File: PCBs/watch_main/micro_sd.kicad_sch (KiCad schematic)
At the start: 2 parts, among them IC1002 NVT4858HKZ, J1101 105162-0001

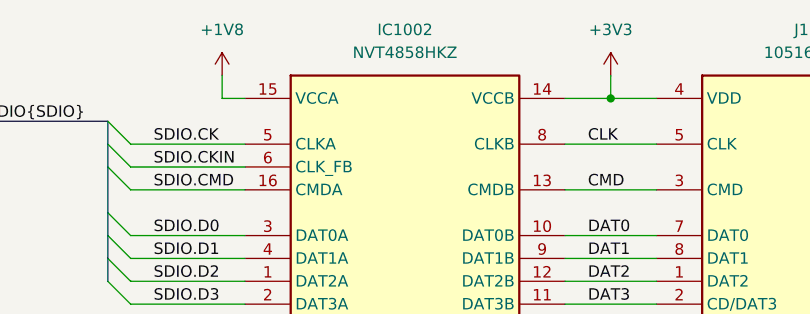
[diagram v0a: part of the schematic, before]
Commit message: Created firmware project
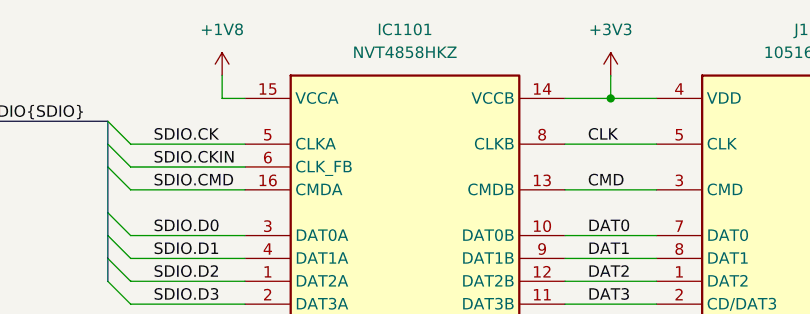
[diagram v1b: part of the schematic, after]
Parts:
- renumbered IC1002 to IC1101
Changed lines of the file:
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@@
   (symbol (lib_id "NVT4858HKZ:NVT4858HKZ") (at 142.24 71.12 0) (unit 1)
     (in_bom yes) (on_board yes) (dnp no)
-    (property "Reference" "IC1002" (at 142.24 50.8 0)
+    (property "Reference" "IC1101" (at 142.24 50.8 0)
       (effects (font (size 1.27 1.27)))
     )
@@
       (project "watch_main"
         (path "/b008648a-c7cf-4e14-8a0a-b9314d757b4a/e2e60111-66fe-4979-9d74-8e725fdfb064"
-          (reference "IC1002") (unit 1)
+          (reference "IC1101") (unit 1)
         )
       )
@@
   (symbol (lib_id "power:GND") (at 208.28 93.98 0) (mirror y) (unit 1)
     (in_bom yes) (on_board yes) (dnp no) (fields_autoplaced)
-    (property "Reference" "#PWR01006" (at 208.28 100.33 0)
+    (property "Reference" "#PWR01105" (at 208.28 100.33 0)
       (effects (font (size 1.27 1.27)) hide)
     )
@@
       (project "watch_main"
         (path "/b008648a-c7cf-4e14-8a0a-b9314d757b4a/e2e60111-66fe-4979-9d74-8e725fdfb064"
-          (reference "#PWR01006") (unit 1)
+          (reference "#PWR01105") (unit 1)
         )
       )
@@
   (symbol (lib_id "power:GND") (at 121.92 88.9 0) (unit 1)
     (in_bom yes) (on_board yes) (dnp no) (fields_autoplaced)
-    (property "Reference" "#PWR01007" (at 121.92 95.25 0)
+    (property "Reference" "#PWR01102" (at 121.92 95.25 0)
       (effects (font (size 1.27 1.27)) hide)
     )
@@
       (project "watch_main"
         (path "/b008648a-c7cf-4e14-8a0a-b9314d757b4a/e2e60111-66fe-4979-9d74-8e725fdfb064"
-          (reference "#PWR01007") (unit 1)
+          (reference "#PWR01102") (unit 1)
         )
       )
@@
   (symbol (lib_id "power:GND") (at 167.64 93.98 0) (unit 1)
     (in_bom yes) (on_board yes) (dnp no) (fields_autoplaced)
-    (property "Reference" "#PWR01005" (at 167.64 100.33 0)
+    (property "Reference" "#PWR01104" (at 167.64 100.33 0)
       (effects (font (size 1.27 1.27)) hide)
     )
@@
       (project "watch_main"
         (path "/b008648a-c7cf-4e14-8a0a-b9314d757b4a/e2e60111-66fe-4979-9d74-8e725fdfb064"
-          (reference "#PWR01005") (unit 1)
+          (reference "#PWR01104") (unit 1)
         )
       )
@@
   (symbol (lib_id "power:+3V3") (at 165.1 55.88 0) (unit 1)
     (in_bom yes) (on_board yes) (dnp no) (fields_autoplaced)
-    (property "Reference" "#PWR01004" (at 165.1 59.69 0)
+    (property "Reference" "#PWR01103" (at 165.1 59.69 0)
       (effects (font (size 1.27 1.27)) hide)
     )
@@
       (project "watch_main"
         (path "/b008648a-c7cf-4e14-8a0a-b9314d757b4a/e2e60111-66fe-4979-9d74-8e725fdfb064"
-          (reference "#PWR01004") (unit 1)
+          (reference "#PWR01103") (unit 1)
         )
       )
@@
   (symbol (lib_id "power:+1V8") (at 121.92 55.88 0) (unit 1)
     (in_bom yes) (on_board yes) (dnp no) (fields_autoplaced)
-    (property "Reference" "#PWR01003" (at 121.92 59.69 0)
+    (property "Reference" "#PWR01101" (at 121.92 59.69 0)
       (effects (font (size 1.27 1.27)) hide)
     )
@@
       (project "watch_main"
         (path "/b008648a-c7cf-4e14-8a0a-b9314d757b4a/e2e60111-66fe-4979-9d74-8e725fdfb064"
-          (reference "#PWR01003") (unit 1)
+          (reference "#PWR01101") (unit 1)
         )
       )

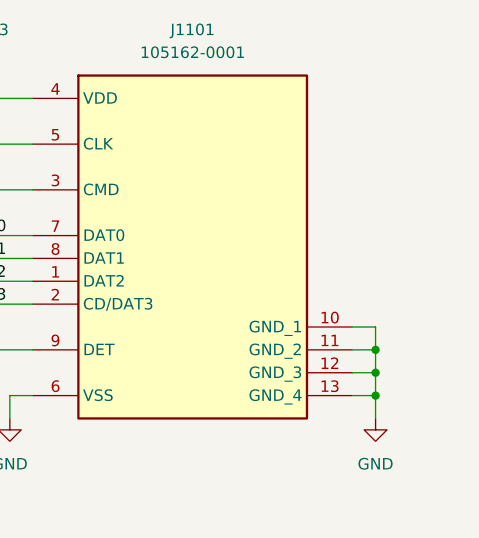
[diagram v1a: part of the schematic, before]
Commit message: Progress with schematic and RFID simulations
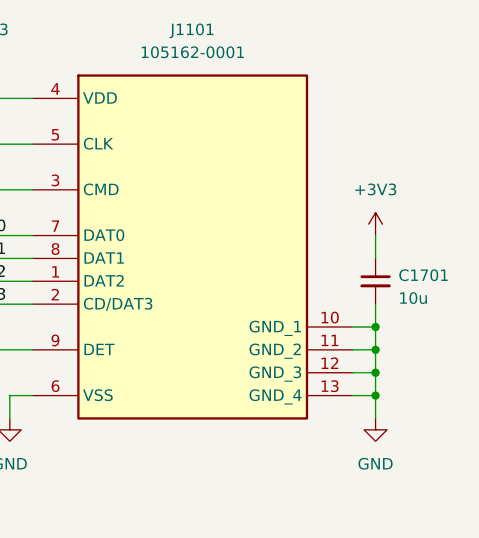
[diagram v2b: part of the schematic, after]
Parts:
- added C1701: 10u, Capacitor_SMD:C_0402_1005Metric, symbol Device:C_Small
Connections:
- net +3V3: now also C1701.1
- net GND: now also C1701.2
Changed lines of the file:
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@@
   (junction (at 208.28 91.44) (diameter 0) (color 0 0 0 0)
   )
+  (junction (at 208.28 83.82) (diameter 0) (color 0 0 0 0)
+  )
   (bus_entry (at 109.22 78.74) (size 2.54 2.54)
     (stroke (width 0) (type default))
@@
     (stroke (width 0) (type default))
   )
+  (wire (pts (xy 208.28 81.28) (xy 208.28 83.82))
+    (stroke (width 0) (type default))
+  )
   (wire (pts (xy 111.76 76.2) (xy 124.46 76.2))
     (stroke (width 0) (type default))
@@
   )
   (wire (pts (xy 111.76 63.5) (xy 124.46 63.5))
+    (stroke (width 0) (type default))
+  )
+  (wire (pts (xy 208.28 73.66) (xy 208.28 76.2))
     (stroke (width 0) (type default))
   )
@@
     )
   )
+  (symbol (lib_id "Device:C_Small") (at 208.28 78.74 0) (unit 1)
+    (in_bom yes) (on_board yes) (dnp no) (fields_autoplaced)
+    (property "Reference" "C1701" (at 210.82 78.1113 0)
+      (effects (font (size 1.27 1.27)) (justify left))
+    )
+    (property "Value" "10u" (at 210.82 80.6513 0)
+      (effects (font (size 1.27 1.27)) (justify left))
+    )
+    (property "Footprint" "Capacitor_SMD:C_0402_1005Metric" (at 208.28 78.74 0)
+      (effects (font (size 1.27 1.27)) hide)
+    )
+    (property "Datasheet" "~" (at 208.28 78.74 0)
+      (effects (font (size 1.27 1.27)) hide)
+    )
+    (pin "1")
+    (pin "2")
+    (instances
+      (project "watch_main"
+        (path "/b008648a-c7cf-4e14-8a0a-b9314d757b4a/e805c593-17ac-4f08-b6e2-d497b0af0a05"
+          (reference "C1701") (unit 1)
+        )
+        (path "/b008648a-c7cf-4e14-8a0a-b9314d757b4a/e2e60111-66fe-4979-9d74-8e725fdfb064"
+          (reference "C1101") (unit 1)
+        )
+      )
+    )
+  )
   (symbol (lib_id "power:+3V3") (at 165.1 55.88 0) (unit 1)
     (in_bom yes) (on_board yes) (dnp no) (fields_autoplaced)
@@
         )
       )
+    )
+  )
+  (symbol (lib_id "power:+3V3") (at 208.28 73.66 0) (unit 1)
+    (in_bom yes) (on_board yes) (dnp no) (fields_autoplaced)
+    (property "Reference" "#PWR01106" (at 208.28 77.47 0)
+      (effects (font (size 1.27 1.27)) hide)
+    )
+    (property "Value" "+3V3" (at 208.28 68.58 0)
+      (effects (font (size 1.27 1.27)))
+    )
+    (property "Footprint" "" (at 208.28 73.66 0)
+      (effects (font (size 1.27 1.27)) hide)
+    )
+    (property "Datasheet" "" (at 208.28 73.66 0)
+      (effects (font (size 1.27 1.27)) hide)
+    )
+    (pin "1")
+    (instances
+      (project "watch_main"
+        (path "/b008648a-c7cf-4e14-8a0a-b9314d757b4a/e2e60111-66fe-4979-9d74-8e725fdfb064"
+          (reference "#PWR01106") (unit 1)
+        )
+      )

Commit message: Started routing main PCB
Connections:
- net GND: now also J1101.14 (MP1), J1101.15 (MP2)
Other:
- note removed: "TODO: Pullup DET?"
- title: (none) -> Watch Micro SD
- moved on the sheet: C1701
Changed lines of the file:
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@@
   (paper "A4")
   (title_block
+    (title "Watch Micro SD")
     (rev "1")
+    (comment 1 "Checked by Ben Smith 21/12/23")
   )
   (junction (at 208.28 86.36) (diameter 0) (color 0 0 0 0)
@@
   (junction (at 165.1 58.42) (diameter 0) (color 0 0 0 0)
   )
+  (junction (at 208.28 78.74) (diameter 0) (color 0 0 0 0)
+  )
   (junction (at 208.28 88.9) (diameter 0) (color 0 0 0 0)
   )
+  (junction (at 208.28 76.2) (diameter 0) (color 0 0 0 0)
+  )
   (junction (at 208.28 91.44) (diameter 0) (color 0 0 0 0)
   )
@@
     (stroke (width 0) (type default))
   )
-  (wire (pts (xy 208.28 81.28) (xy 208.28 83.82))
+  (wire (pts (xy 208.28 73.66) (xy 208.28 76.2))
     (stroke (width 0) (type default))
   )
@@
     (stroke (width 0) (type default))
   )
+  (wire (pts (xy 208.28 76.2) (xy 208.28 78.74))
+    (stroke (width 0) (type default))
+  )
   (wire (pts (xy 111.76 78.74) (xy 124.46 78.74))
     (stroke (width 0) (type default))
@@
     (stroke (width 0) (type default))
   )
-  (wire (pts (xy 208.28 73.66) (xy 208.28 76.2))
+  (wire (pts (xy 208.28 66.04) (xy 208.28 68.58))
     (stroke (width 0) (type default))
   )
@@
     (stroke (width 0) (type default))
   )
+  (wire (pts (xy 205.74 76.2) (xy 208.28 76.2))
+    (stroke (width 0) (type default))
+  )
   (wire (pts (xy 165.1 55.88) (xy 165.1 58.42))
     (stroke (width 0) (type default))
@@
     (stroke (width 0) (type default))
   )
+  (wire (pts (xy 208.28 78.74) (xy 208.28 83.82))
+    (stroke (width 0) (type default))
+  )
   (wire (pts (xy 167.64 91.44) (xy 170.18 91.44))
     (stroke (width 0) (type default))
@@
     (stroke (width 0) (type default))
   )
+  (wire (pts (xy 205.74 78.74) (xy 208.28 78.74))
+    (stroke (width 0) (type default))
+  )
   (wire (pts (xy 160.02 76.2) (xy 170.18 76.2))
     (stroke (width 0) (type default))
@@
   (wire (pts (xy 160.02 63.5) (xy 170.18 63.5))
     (stroke (width 0) (type default))
-  )
-  (text "TODO: Pullup DET?" (at 180.34 170.18 0)
-    (effects (font (size 1.27 1.27)) (justify left bottom))
   )
   (text "CD needs to be\npulled up by host" (at 66.04 99.06 0)
@@
   (symbol (lib_id "power:GND") (at 208.28 93.98 0) (mirror y) (unit 1)
     (in_bom yes) (on_board yes) (dnp no) (fields_autoplaced)
-    (property "Reference" "#PWR01105" (at 208.28 100.33 0)
+    (property "Reference" "#PWR01106" (at 208.28 100.33 0)
       (effects (font (size 1.27 1.27)) hide)
     )
@@
       (project "watch_main"
         (path "/b008648a-c7cf-4e14-8a0a-b9314d757b4a/e2e60111-66fe-4979-9d74-8e725fdfb064"
-          (reference "#PWR01105") (unit 1)
+          (reference "#PWR01106") (unit 1)
         )
       )
@@
     )
   )
-  (symbol (lib_id "Device:C_Small") (at 208.28 78.74 0) (unit 1)
-    (in_bom yes) (on_board yes) (dnp no) (fields_autoplaced)
-    (property "Reference" "C1701" (at 210.82 78.1113 0)
+  (symbol (lib_id "Device:C_Small") (at 208.28 71.12 0) (unit 1)
+    (in_bom yes) (on_board yes) (dnp no) (fields_autoplaced)
+    (property "Reference" "C1701" (at 210.82 70.4913 0)
       (effects (font (size 1.27 1.27)) (justify left))
     )
-    (property "Value" "10u" (at 210.82 80.6513 0)
+    (property "Value" "10u" (at 210.82 73.0313 0)
       (effects (font (size 1.27 1.27)) (justify left))
     )
-    (property "Footprint" "Capacitor_SMD:C_0402_1005Metric" (at 208.28 78.74 0)
-      (effects (font (size 1.27 1.27)) hide)
-    )
-    (property "Datasheet" "~" (at 208.28 78.74 0)
+    (property "Footprint" "Capacitor_SMD:C_0402_1005Metric" (at 208.28 71.12 0)
+      (effects (font (size 1.27 1.27)) hide)
+    )
+    (property "Datasheet" "~" (at 208.28 71.12 0)
       (effects (font (size 1.27 1.27)) hide)
     )
@@
     )
   )
-  (symbol (lib_id "power:+3V3") (at 208.28 73.66 0) (unit 1)
-    (in_bom yes) (on_board yes) (dnp no) (fields_autoplaced)
-    (property "Reference" "#PWR01106" (at 208.28 77.47 0)
-      (effects (font (size 1.27 1.27)) hide)
-    )
-    (property "Value" "+3V3" (at 208.28 68.58 0)
-      (effects (font (size 1.27 1.27)))
-    )
-    (property "Footprint" "" (at 208.28 73.66 0)
-      (effects (font (size 1.27 1.27)) hide)
-    )
-    (property "Datasheet" "" (at 208.28 73.66 0)
-      (effects (font (size 1.27 1.27)) hide)
-    )
-    (pin "1")
-    (instances
-      (project "watch_main"
-        (path "/b008648a-c7cf-4e14-8a0a-b9314d757b4a/e2e60111-66fe-4979-9d74-8e725fdfb064"
-          (reference "#PWR01106") (unit 1)
+  (symbol (lib_id "power:+3V3") (at 208.28 66.04 0) (unit 1)
+    (in_bom yes) (on_board yes) (dnp no) (fields_autoplaced)
+    (property "Reference" "#PWR01105" (at 208.28 69.85 0)
+      (effects (font (size 1.27 1.27)) hide)
+    )
+    (property "Value" "+3V3" (at 208.28 60.96 0)
+      (effects (font (size 1.27 1.27)))
+    )
+    (property "Footprint" "" (at 208.28 66.04 0)
+      (effects (font (size 1.27 1.27)) hide)
+    )
+    (property "Datasheet" "" (at 208.28 66.04 0)
+      (effects (font (size 1.27 1.27)) hide)
+    )
+    (pin "1")
+    (instances
+      (project "watch_main"
+        (path "/b008648a-c7cf-4e14-8a0a-b9314d757b4a/e2e60111-66fe-4979-9d74-8e725fdfb064"
+          (reference "#PWR01105") (unit 1)
         )
       )
@@
     (pin "12")
     (pin "13")
+    (pin "14")
+    (pin "15")
     (pin "2")
     (pin "3")

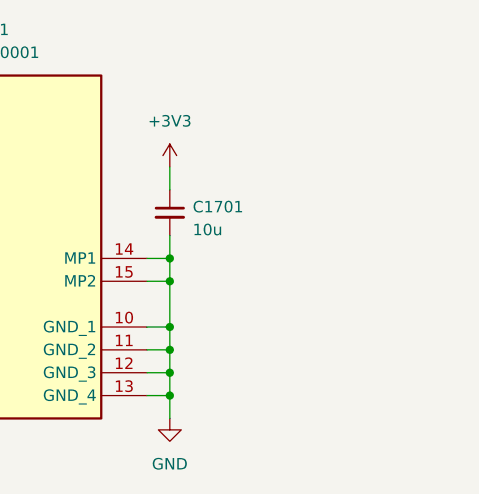
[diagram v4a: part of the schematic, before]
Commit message: 287 Connections unrouted
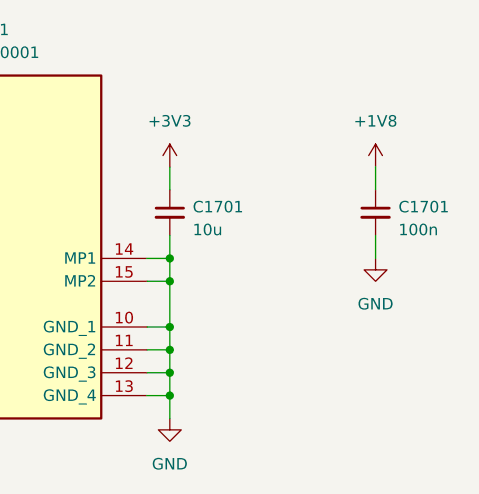
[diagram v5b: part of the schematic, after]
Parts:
- added C1701: 100n, Capacitor_SMD:C_0402_1005Metric, symbol Device:C_Small
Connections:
- net +1V8: now also C1701.1
- net GND: now also C1701.2
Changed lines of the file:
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@@
+    (stroke (width 0) (type default))
+  )
+  (wire (pts (xy 231.14 66.04) (xy 231.14 68.58))
     (stroke (width 0) (type default))
   )
@@
   )
   (wire (pts (xy 160.02 76.2) (xy 170.18 76.2))
+    (stroke (width 0) (type default))
+  )
+  (wire (pts (xy 231.14 73.66) (xy 231.14 76.2))
     (stroke (width 0) (type default))
   )
@@
     )
   )
+  (symbol (lib_id "Device:C_Small") (at 231.14 71.12 0) (unit 1)
+    (in_bom yes) (on_board yes) (dnp no) (fields_autoplaced)
+    (property "Reference" "C1701" (at 233.68 70.4913 0)
+      (effects (font (size 1.27 1.27)) (justify left))
+    )
+    (property "Value" "100n" (at 233.68 73.0313 0)
+      (effects (font (size 1.27 1.27)) (justify left))
+    )
+    (property "Footprint" "Capacitor_SMD:C_0402_1005Metric" (at 231.14 71.12 0)
+      (effects (font (size 1.27 1.27)) hide)
+    )
+    (property "Datasheet" "~" (at 231.14 71.12 0)
+      (effects (font (size 1.27 1.27)) hide)
+    )
+    (pin "1")
+    (pin "2")
+    (instances
+      (project "watch_main"
+        (path "/b008648a-c7cf-4e14-8a0a-b9314d757b4a/e805c593-17ac-4f08-b6e2-d497b0af0a05"
+          (reference "C1701") (unit 1)
+        )
+        (path "/b008648a-c7cf-4e14-8a0a-b9314d757b4a/e2e60111-66fe-4979-9d74-8e725fdfb064"
+          (reference "C1102") (unit 1)
+        )
+      )
+    )
+  )
   (symbol (lib_id "power:GND") (at 208.28 93.98 0) (mirror y) (unit 1)
     (in_bom yes) (on_board yes) (dnp no) (fields_autoplaced)
@@
         (path "/b008648a-c7cf-4e14-8a0a-b9314d757b4a/e2e60111-66fe-4979-9d74-8e725fdfb064"
           (reference "#PWR01106") (unit 1)
+        )
+      )
+    )
+  )
+  (symbol (lib_id "power:+1V8") (at 231.14 66.04 0) (unit 1)
+    (in_bom yes) (on_board yes) (dnp no) (fields_autoplaced)
+    (property "Reference" "#PWR01107" (at 231.14 69.85 0)
+      (effects (font (size 1.27 1.27)) hide)
+    )
+    (property "Value" "+1V8" (at 231.14 60.96 0)
+      (effects (font (size 1.27 1.27)))
+    )
+    (property "Footprint" "" (at 231.14 66.04 0)
+      (effects (font (size 1.27 1.27)) hide)
+    )
+    (property "Datasheet" "" (at 231.14 66.04 0)
+      (effects (font (size 1.27 1.27)) hide)
+    )
+    (pin "1")
+    (instances
+      (project "watch_main"
+        (path "/b008648a-c7cf-4e14-8a0a-b9314d757b4a/e2e60111-66fe-4979-9d74-8e725fdfb064"
+          (reference "#PWR01107") (unit 1)
         )
       )
@@
         )
       )
+    )
+  )
+  (symbol (lib_id "power:GND") (at 231.14 76.2 0) (mirror y) (unit 1)
+    (in_bom yes) (on_board yes) (dnp no) (fields_autoplaced)
+    (property "Reference" "#PWR01108" (at 231.14 82.55 0)
+      (effects (font (size 1.27 1.27)) hide)
+    )
+    (property "Value" "GND" (at 231.14 81.28 0)
+      (effects (font (size 1.27 1.27)))
+    )
+    (property "Footprint" "" (at 231.14 76.2 0)
+      (effects (font (size 1.27 1.27)) hide)
+    )
+    (property "Datasheet" "" (at 231.14 76.2 0)
+      (effects (font (size 1.27 1.27)) hide)
+    )
+    (pin "1")
+    (instances
+      (project "watch_main"
+        (path "/b008648a-c7cf-4e14-8a0a-b9314d757b4a/e2e60111-66fe-4979-9d74-8e725fdfb064"
+          (reference "#PWR01108") (unit 1)
+        )
+      )
